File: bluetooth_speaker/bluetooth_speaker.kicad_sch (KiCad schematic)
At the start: 22 parts, among them U1 MAX98357A, U2 XL4015, U3 ESP32-WROOM-32UE

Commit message: Refactor
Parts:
- removed C1: 10µF, symbol Device:C_Small
- removed C2: 0.1µF, symbol Device:C_Small
- removed C3, C6, C7: 1µF, symbol Device:C_Small
- removed C4: 330µF/25V, symbol Device:C_Small_US
- removed C8: 220µF/50V, symbol Device:C_Small_US
- removed D2: MBR1045, Package_TO_SOT_THT:TO-220-2_Horizontal_TabDown, symbol Diode:MBR745
- removed L1: 47µH/5A, symbol Device:L
- removed LS1: Speaker, symbol Device:Speaker
- removed R1: 300kΩ, symbol Device:R_US
- removed R2: 16.5kΩ, symbol Device:R_US
- removed R3, R4, R5: 10kΩ, symbol Device:R_US
- removed U1: MAX98357A, Package_DFN_QFN:TQFN-16-1EP_3x3mm_P0.5mm_EP1.23x1.23mm, symbol Audio:MAX98357A
- removed U2: XL4015, Package_TO_SOT_SMD:TO-263-5_TabPin3, symbol Regulator_Switching:XL4015
- removed U3: ESP32-WROOM-32UE, RF_Module:ESP32-WROOM-32UE, symbol RF_Module:ESP32-WROOM-32UE
- added C12, C15: 0.1µF, symbol Device:C_Small
- added C13: 10µF, symbol Device:C_Small
- added C14, C18: 1µF, symbol Device:C_Small
- added C16, C17: 1.5pF, symbol Device:C_Small
- added J1: Conn_Coaxial, symbol Connector:Conn_Coaxial
- added L2: 2nH(0.1nH), symbol Device:L
- added L3: 2.7nH, symbol Device:L
- added U4: ESP32-D0WD-V3, QFN48_ESP32-D0WD-V3_EXP, symbol ESP32-D0WD-V3:ESP32-D0WD-V3
- added U5: 282836-4, 282836-4_TYC, symbol 282836-4:282836-4
- C10: value 1µF -> 0.1µF
- C11: value 1µF -> 100pF
- C5: value 33nF -> 0.1µF
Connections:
- net GNDREF is gone; now on net GND: C10.2, C11.2, C9.2
- net Vdd33 is gone; now on net +3.3V: C10.1, C5.1, C9.1
- net DATA: now also U4.39 (GPIO22)
- net LRCLK: now also U4.14 (GPIO25)
- net SD_MODE: now also U4.16 (GPIO27)
- net GND: now reaches C5.2
- net GND: now also C12.2, C13.2, C14.2, C15.2, C16.2, C17.2, C18.2, J1.2 (Ext), U4.49 (GND)
- net +3.3V: now reaches C11.1
- net +3.3V: now also C12.1, C13.1, C14.1, C15.1, C18.1, L2.1, U4.1 (VDDA), U4.19 (VDD3P3_RTC), U4.26 (VDD_SDIO), U4.37 (VDD3P3_CPU), U4.43 (VDDA), U4.46 (VDDA)
- new net: C17.1, J1.1 (In), L3.2
- new net: L2.2, U4.3 (VDD3P3), U4.4 (VDD3P3)
- new net Audio/AUDIO_OUT+: U5.3
- new net Audio/AUDIO_OUT-: U5.4
- new net BCLK: U4.15 (GPIO26)
- new net LNA_IN: C16.1, L3.1, U4.2 (LNA_IN)
- new net Power/Batt+: U5.1
- new net Power/Batt-: U5.2
- new net XTAL_N: U4.44 (XTAL_N)
- new net XTAL_P: U4.45 (XTAL_P)
- no-connect marks 22 -> 33
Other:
- added sheet Audio (audio.kicad_sch)
- added sheet Power (power.kicad_sch)
- note added: "antenna"
- note added: "terminal"

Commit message: Updated schematic
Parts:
- added C19, C20: 10pF, symbol Device:C_Small
- added J2: USB_C_Receptacle_USB2.0_16P, Connector_USB:USB_C_Receptacle_GCT_USB4085, symbol Connector:USB_C_Receptacle_USB2.0_16P
- added L4: 2nH(0.1nH), symbol Device:L
- added Y1: 40MHz(±10 ppm), Crystal:Crystal_SMD_SeikoEpson_MC306-4Pin_8.0x3.2mm, symbol Device:Crystal_GND24
- U4: footprint QFN48_ESP32-D0WD-V3_EXP -> ESP32-D0WD-V3:QFN48_ESP32-D0WD-V3_EXP
- U5: footprint 282836-4_TYC -> 282836-4:282836-4_TYC
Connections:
- net GND: now also C19.2, C20.1, J2.A1 (GND), J2.A12 (GND), J2.B1 (GND), J2.B12 (GND), J2.S1 (SHIELD), Y1.2, Y1.4
- net XTAL_N: now also C19.1, Y1.3
- net XTAL_P: now also L4.1
- net U0RXD: now reaches U4.40 (U0RXD)
- net U0TXD: now reaches U4.41 (U0TXD)
- new net: C20.2, L4.2, Y1.1
- new net USB-UART Converter/USB_D+: J2.A6 (D+), J2.B6 (D+)
- new net USB-UART Converter/USB_D-: J2.A7 (D-), J2.B7 (D-)
- new net USB-UART Converter/VBUS: J2.A4 (VBUS), J2.A9 (VBUS), J2.B4 (VBUS), J2.B9 (VBUS)
- no-connect marks 33 -> 35
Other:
- added sheet USB-UART Converter (usb-uart_converter.kicad_sch)
- note added: "CRYSTAL"
- note added: "USB-C connector"

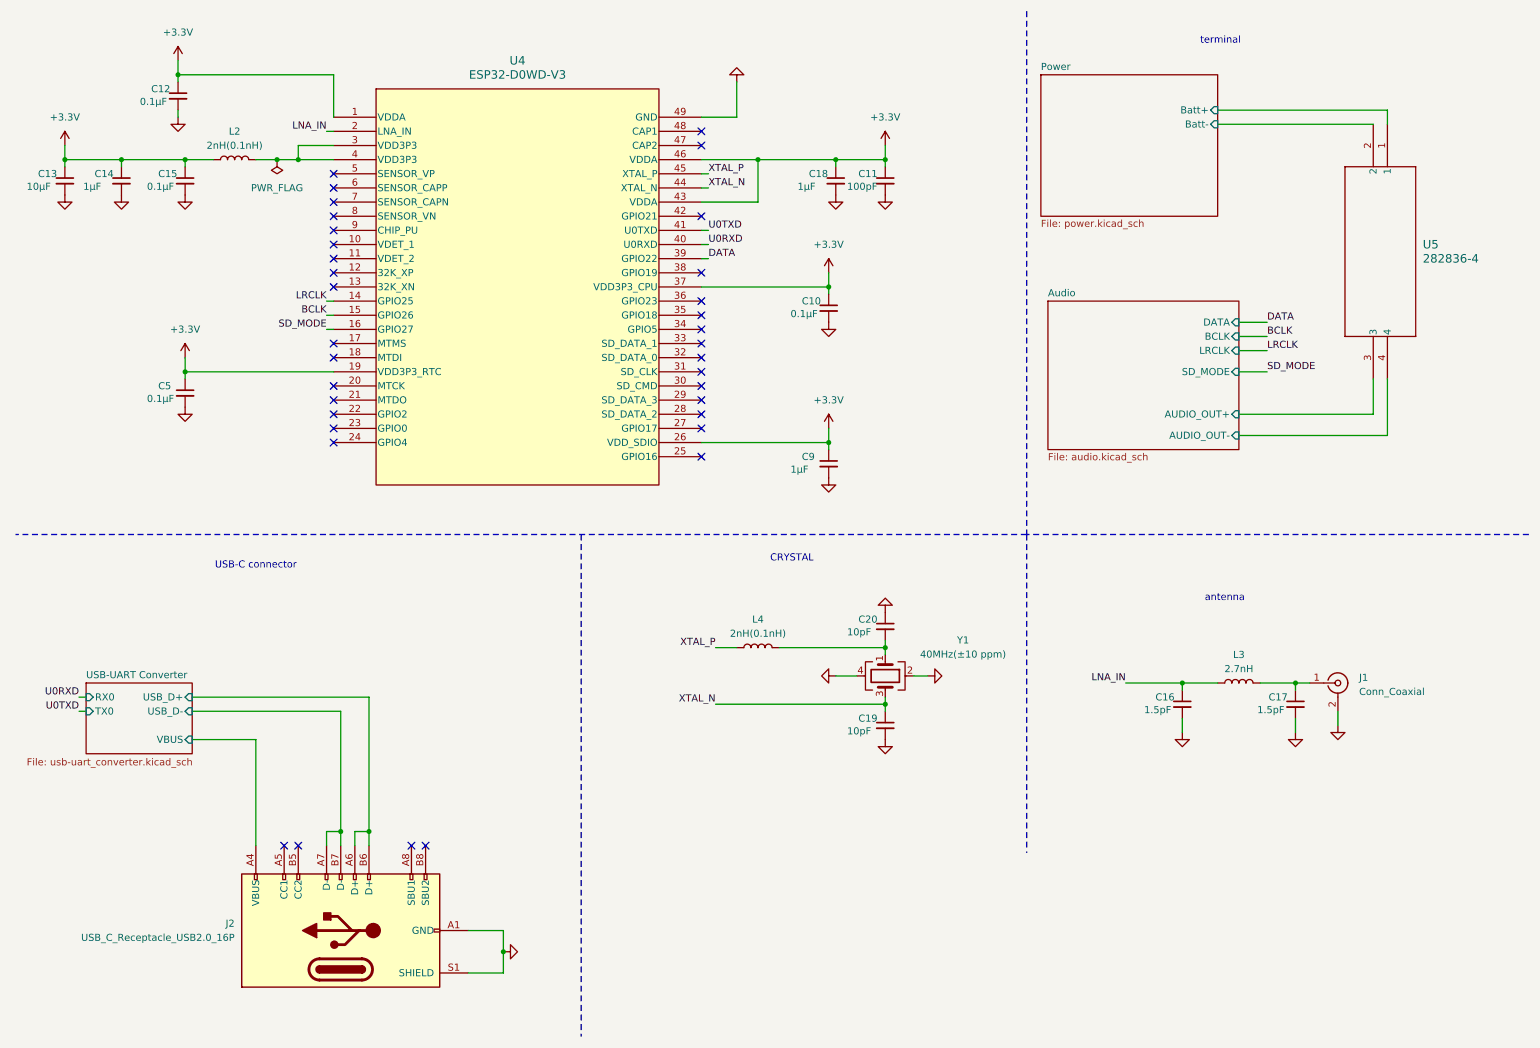
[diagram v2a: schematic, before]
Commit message: adding few footprints
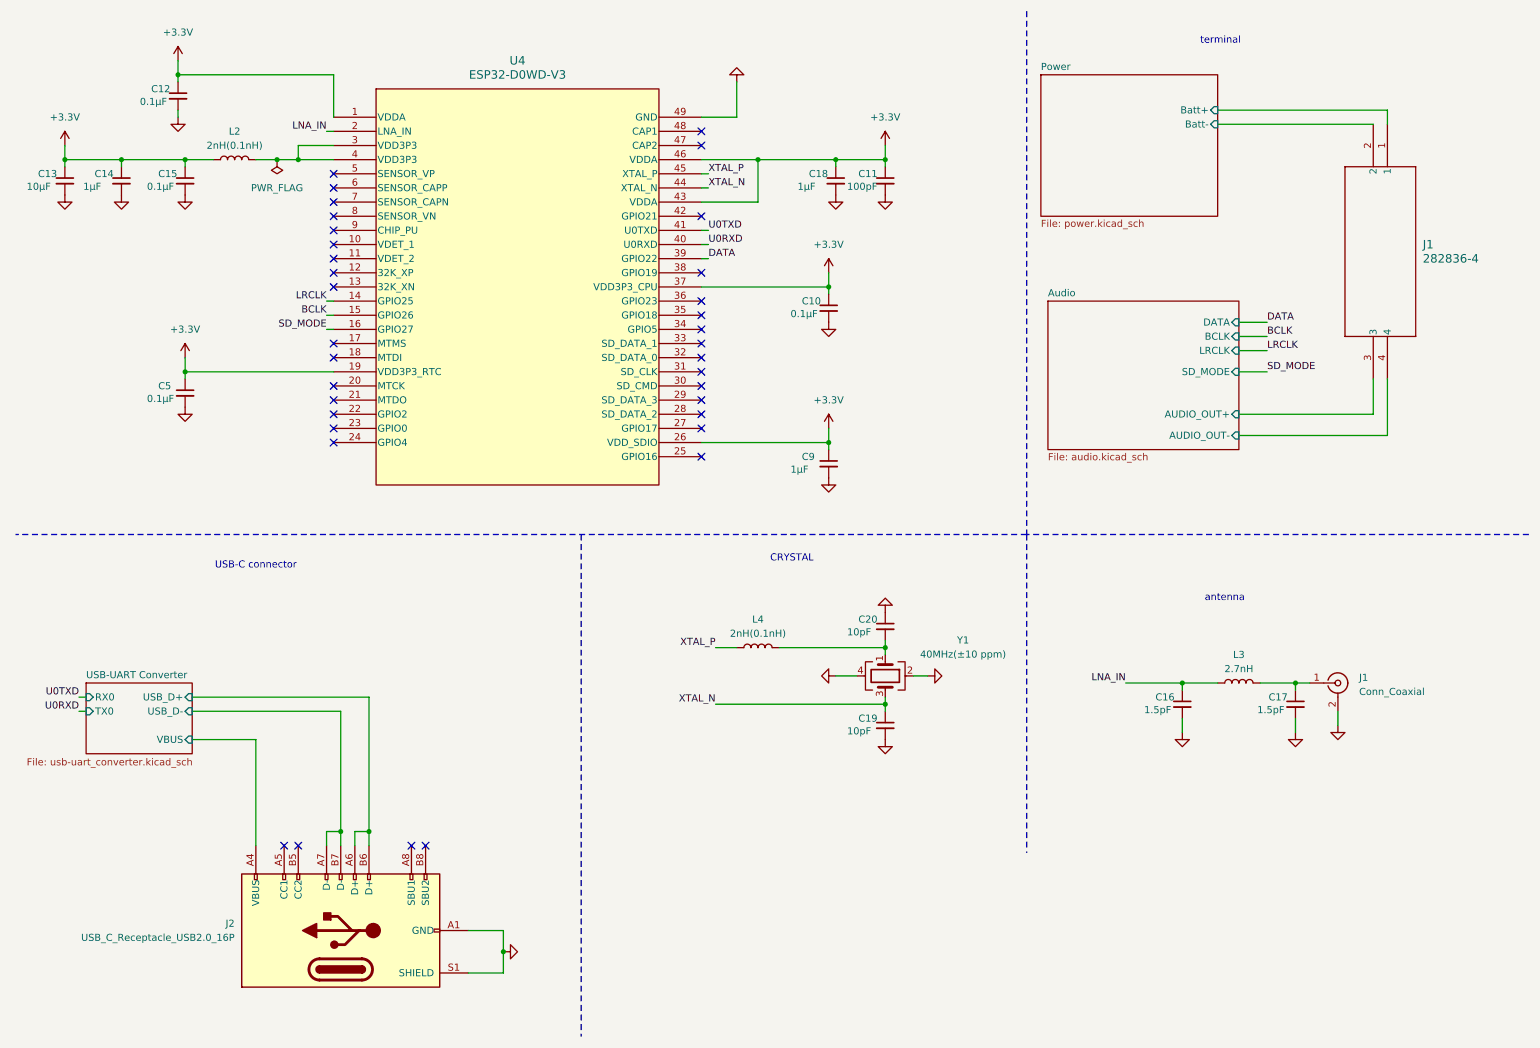
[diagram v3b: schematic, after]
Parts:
- C10, C11, C12, C13, C14, C15, C16, C17, C18, C19, C20, C9: footprint (none) -> Capacitor_SMD:C_0603_1608Metric_Pad1.08x0.95mm_HandSolder
- renumbered U5 to J1
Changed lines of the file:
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@@
 		)
 	)
-	(label "U0RXD"
+	(label "U0TXD"
 		(at 24.13 135.89 180)
 		(effects
@@
 		)
 	)
-	(label "U0TXD"
+	(label "U0RXD"
 		(at 24.13 138.43 180)
 		(effects
@@
 			)
 		)
-		(property "Footprint" ""
+		(property "Footprint" "Capacitor_SMD:C_0603_1608Metric_Pad1.08x0.95mm_HandSolder"
 			(at 242.57 137.16 0)
 			(effects
@@
 			)
 		)
-		(property "Footprint" ""
+		(property "Footprint" "Capacitor_SMD:C_0603_1608Metric_Pad1.08x0.95mm_HandSolder"
 			(at 21.59 43.18 0)
 			(effects
@@
 			)
 		)
-		(property "Footprint" ""
+		(property "Footprint" "Capacitor_SMD:C_0603_1608Metric_Pad1.08x0.95mm_HandSolder"
 			(at 43.18 43.18 0)
 			(effects
@@
 			)
 		)
-		(property "Footprint" ""
+		(property "Footprint" "Capacitor_SMD:C_0603_1608Metric_Pad1.08x0.95mm_HandSolder"
 			(at 160.02 43.18 0)
 			(effects
@@
 		(dnp no)
 		(fields_autoplaced yes)
-		(property "Reference" "U5"
+		(property "Reference" "J1"
 			(at 265.43 54.6099 90)
 			(effects
@@
 			(project ""
 				(path "/13ff5fb5-140a-4554-92d9-4ae3849ea082"
-					(reference "U5")
+					(reference "J1")
 					(unit 1)
 				)
@@
 			)
 		)
-		(property "Footprint" ""
+		(property "Footprint" "Capacitor_SMD:C_0603_1608Metric_Pad1.08x0.95mm_HandSolder"
 			(at 168.91 43.18 0)
 			(effects
@@
 			)
 		)
-		(property "Footprint" ""
+		(property "Footprint" "Capacitor_SMD:C_0603_1608Metric_Pad1.08x0.95mm_HandSolder"
 			(at 158.75 66.04 0)
 			(effects
@@
 			)
 		)
-		(property "Footprint" ""
+		(property "Footprint" "Capacitor_SMD:C_0603_1608Metric_Pad1.08x0.95mm_HandSolder"
 			(at 158.75 93.98 0)
 			(effects
@@
 			)
 		)
-		(property "Footprint" ""
+		(property "Footprint" "Capacitor_SMD:C_0603_1608Metric_Pad1.08x0.95mm_HandSolder"
 			(at 41.91 27.94 0)
 			(effects
@@
 			)
 		)
-		(property "Footprint" ""
+		(property "Footprint" "Capacitor_SMD:C_0603_1608Metric_Pad1.08x0.95mm_HandSolder"
 			(at 168.91 140.97 0)
 			(effects
@@
 			)
 		)
-		(property "Footprint" ""
+		(property "Footprint" "Capacitor_SMD:C_0603_1608Metric_Pad1.08x0.95mm_HandSolder"
 			(at 168.91 123.19 0)
 			(effects
@@
 			)
 		)
-		(property "Footprint" ""
+		(property "Footprint" "Capacitor_SMD:C_0603_1608Metric_Pad1.08x0.95mm_HandSolder"
 			(at 222.25 137.16 0)
 			(effects
@@
 			)
 		)
-		(property "Footprint" ""
+		(property "Footprint" "Capacitor_SMD:C_0603_1608Metric_Pad1.08x0.95mm_HandSolder"
 			(at 31.75 43.18 0)
 			(effects

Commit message: Completed adding footprints, set up PCB rules
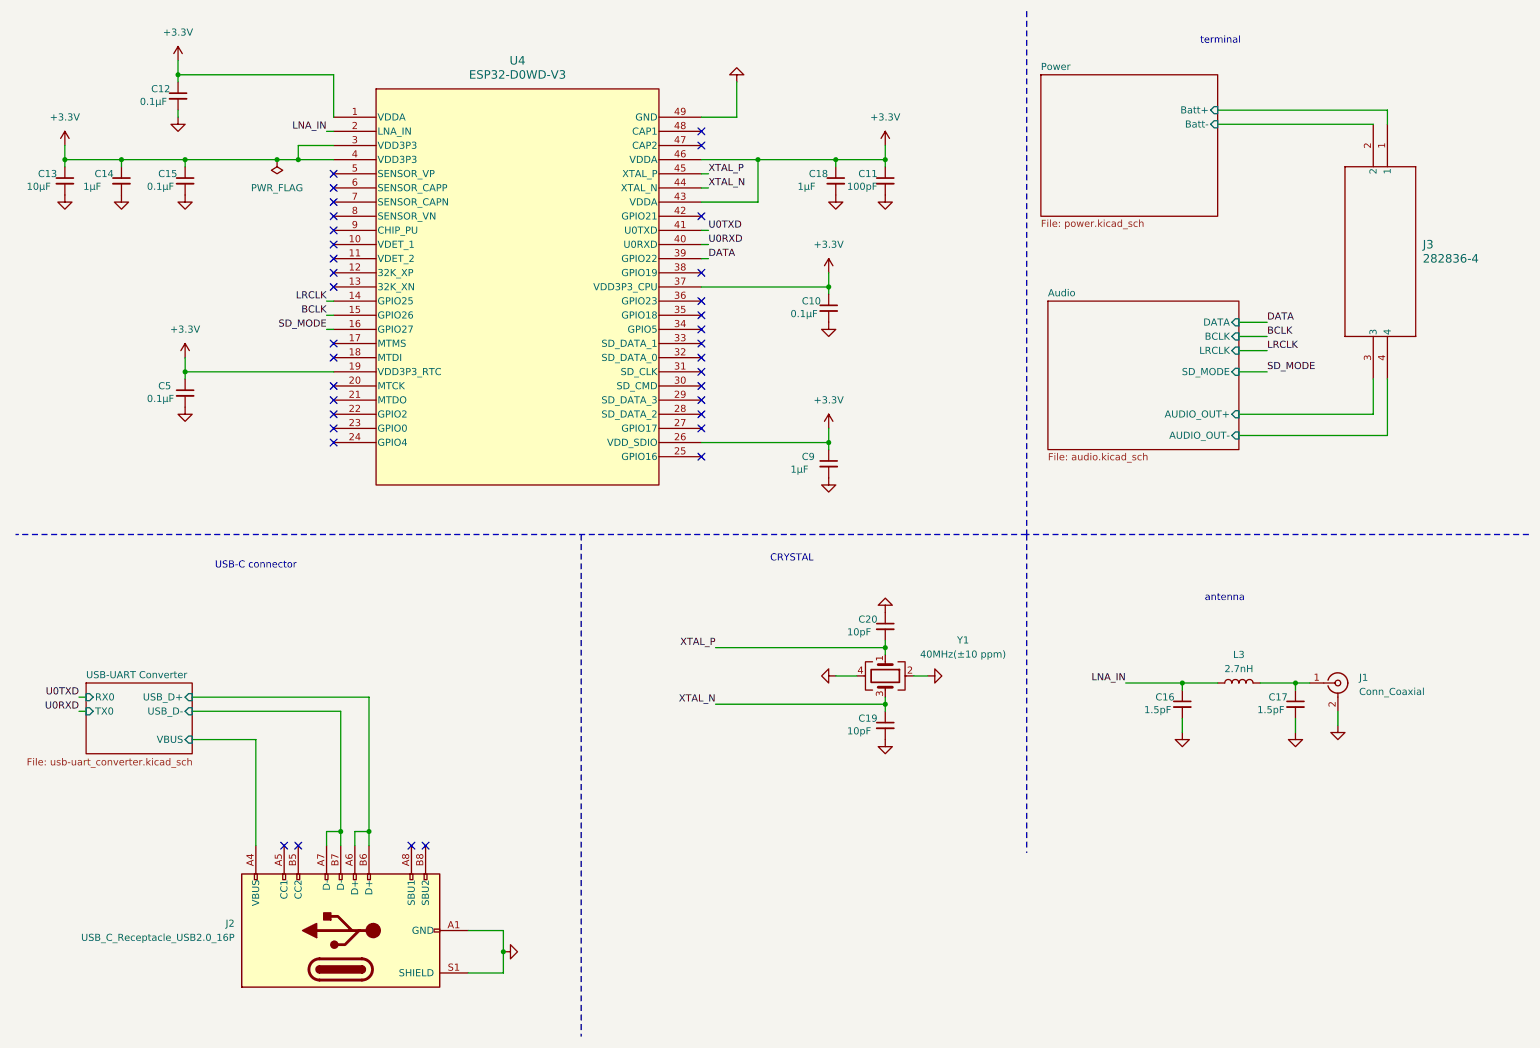
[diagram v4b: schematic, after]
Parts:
- removed L2, L4: 2nH(0.1nH), symbol Device:L
- C16, C17: footprint Capacitor_SMD:C_0603_1608Metric_Pad1.08x0.95mm_HandSolder -> SamacSys_Parts:GRM033D70J224ME01D
- C5: footprint (none) -> Capacitor_SMD:C_0603_1608Metric_Pad1.08x0.95mm_HandSolder
- J1: footprint (none) -> Connector_Coaxial:SMA_Samtec_SMA-J-P-H-ST-EM1_EdgeMount
- L3: footprint (none) -> SamacSys_Parts:LQP03TG3N1B02D
- renumbered J1 to J3
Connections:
- net +3.3V: now also U4.3 (VDD3P3), U4.4 (VDD3P3)
- net XTAL_P: now also C20.2, Y1.1
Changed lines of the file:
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@@
 	(wire
 		(pts
-			(xy 149.86 127) (xy 168.91 127)
-		)
-		(stroke
-			(width 0)
-			(type default)
-		)
-	)
-	(wire
-		(pts
 			(xy 212.09 133.35) (xy 222.25 133.35)
 		)
@@
 	(wire
 		(pts
-			(xy 138.43 127) (xy 142.24 127)
+			(xy 138.43 127) (xy 168.91 127)
 		)
 		(stroke
@@
 	(wire
 		(pts
-			(xy 55.88 39.37) (xy 59.69 39.37)
-		)
-		(stroke
-			(width 0)
-			(type default)
-		)
-	)
-	(wire
-		(pts
 			(xy 135.89 90.17) (xy 158.75 90.17)
 		)
@@
 	(wire
 		(pts
-			(xy 43.18 39.37) (xy 48.26 39.37)
+			(xy 43.18 39.37) (xy 59.69 39.37)
 		)
 		(stroke
@@
 			)
 		)
-		(property "Footprint" "Capacitor_SMD:C_0603_1608Metric_Pad1.08x0.95mm_HandSolder"
+		(property "Footprint" "SamacSys_Parts:GRM033D70J224ME01D"
 			(at 242.57 137.16 0)
 			(effects
@@
 			)
 		)
-		(property "Datasheet" "~"
+		(property "Datasheet" "https://www.mouser.pl/datasheet/3/76/1/GRM0335C1H1R0BA01-01A.pdf"
 			(at 242.57 137.16 0)
 			(effects
@@
 			)
 		)
-		(property "Footprint" ""
+		(property "Footprint" "Capacitor_SMD:C_0603_1608Metric_Pad1.08x0.95mm_HandSolder"
 			(at 43.18 81.28 0)
 			(effects
@@
 			)
 		)
-		(property "Footprint" ""
+		(property "Footprint" "Connector_Coaxial:SMA_Samtec_SMA-J-P-H-ST-EM1_EdgeMount"
 			(at 250.19 133.35 0)
 			(effects
@@
 		(dnp no)
 		(fields_autoplaced yes)
-		(property "Reference" "J1"
+		(property "Reference" "J3"
 			(at 265.43 54.6099 90)
 			(effects
@@
 			(project ""
 				(path "/13ff5fb5-140a-4554-92d9-4ae3849ea082"
-					(reference "J1")
+					(reference "J3")
 					(unit 1)
 				)
@@
 	)
 	(symbol
-		(lib_id "Device:L")
-		(at 146.05 127 90)
-		(unit 1)
-		(exclude_from_sim no)
-		(in_bom yes)
-		(on_board yes)
-		(dnp no)
-		(fields_autoplaced yes)
-		(property "Reference" "L4"
-			(at 146.05 121.92 90)
-			(effects
-				(font
-					(size 1.27 1.27)
-				)
-			)
-		)
-		(property "Value" "2nH(0.1nH)"
-			(at 146.05 124.46 90)
-			(effects
-				(font
-					(size 1.27 1.27)
-				)
-			)
-		)
-		(property "Footprint" ""
-			(at 146.05 127 0)
-			(effects
-				(font
-					(size 1.27 1.27)
-				)
-				(hide yes)
-			)
-		)
-		(property "Datasheet" "~"
-			(at 146.05 127 0)
-			(effects
-				(font
-					(size 1.27 1.27)
-				)
-				(hide yes)
-			)
-		)
-		(property "Description" "Inductor"
-			(at 146.05 127 0)
-			(effects
-				(font
-					(size 1.27 1.27)
-				)
-				(hide yes)
-			)
-		)
-		(pin "2"
-		)
-		(pin "1"
-		)
-		(instances
-			(project "bluetooth_speaker"
-				(path "/13ff5fb5-140a-4554-92d9-4ae3849ea082"
-					(reference "L4")
-					(unit 1)
-				)
-			)
-		)
-	)
-	(symbol
 		(lib_id "Device:Crystal_GND24")
 		(at 168.91 132.08 270)
@@
 	)
 	(symbol
-		(lib_id "Device:L")
-		(at 52.07 39.37 90)
-		(unit 1)
-		(exclude_from_sim no)
-		(in_bom yes)
-		(on_board yes)
-		(dnp no)
-		(fields_autoplaced yes)
-		(property "Reference" "L2"
-			(at 52.07 34.29 90)
-			(effects
-				(font
-					(size 1.27 1.27)
-				)
-			)
-		)
-		(property "Value" "2nH(0.1nH)"
-			(at 52.07 36.83 90)
-			(effects
-				(font
-					(size 1.27 1.27)
-				)
-			)
-		)
-		(property "Footprint" ""
-			(at 52.07 39.37 0)
-			(effects
-				(font
-					(size 1.27 1.27)
-				)
-				(hide yes)
-			)
-		)
-		(property "Datasheet" "~"
-			(at 52.07 39.37 0)
-			(effects
-				(font
-					(size 1.27 1.27)
-				)
-				(hide yes)
-			)
-		)
-		(property "Description" "Inductor"
-			(at 52.07 39.37 0)
-			(effects
-				(font
-					(size 1.27 1.27)
-				)
-				(hide yes)
-			)
-		)
-		(pin "2"
-		)
-		(pin "1"
-		)
-		(instances
-			(project ""
-				(path "/13ff5fb5-140a-4554-92d9-4ae3849ea082"
-					(reference "L2")
-					(unit 1)
-				)
-			)
-		)
-	)
-	(symbol
 		(lib_id "power:GND")
 		(at 158.75 68.58 0)
@@
 			)
 		)
-		(property "Footprint" ""
+		(property "Footprint" "SamacSys_Parts:LQP03TG3N1B02D"
 			(at 232.41 133.35 0)
 			(effects
@@
 			)
 		)
-		(property "Datasheet" "~"
+		(property "Datasheet" "https://www.mouser.pl/datasheet/3/76/2/JELF243C_0015.pdf"
 			(at 232.41 133.35 0)
 			(effects
@@
 			)
 		)
-		(property "Footprint" "Capacitor_SMD:C_0603_1608Metric_Pad1.08x0.95mm_HandSolder"
+		(property "Footprint" "SamacSys_Parts:GRM033D70J224ME01D"
 			(at 222.25 137.16 0)
 			(effects
@@
 			)
 		)
-		(property "Datasheet" "~"
+		(property "Datasheet" "https://www.mouser.pl/datasheet/3/76/1/GRM0335C1H1R0BA01-01A.pdf"
 			(at 222.25 137.16 0)
 			(effects
